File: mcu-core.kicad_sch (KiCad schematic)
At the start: 17 parts, among them SW1 B3U-1000P, U1 STM32F103C8T6, Y1 12MHz

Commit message: Modified gitignore
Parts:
- C2: value 4u7 -> 0u1
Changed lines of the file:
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@@
       (effects (font (size 1.27 1.27)) (justify left))
     )
-    (property "Value" "4u7" (id 1) (at 35.56 181.6162 0)
+    (property "Value" "0u1" (id 1) (at 35.56 181.6162 0)
       (effects (font (size 1.27 1.27)) (justify left))
     )

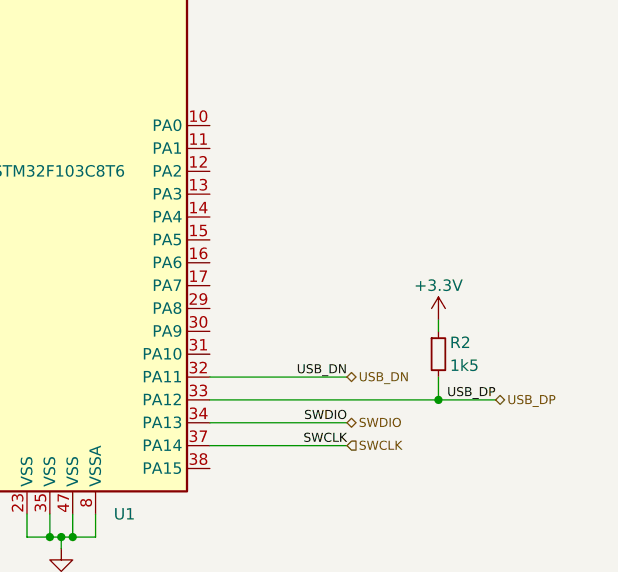
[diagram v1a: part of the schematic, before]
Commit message: Added connections for motor 2
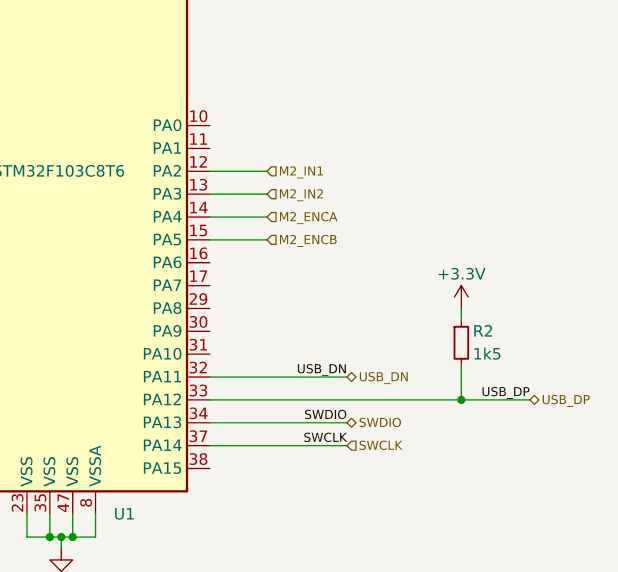
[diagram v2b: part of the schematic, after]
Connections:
- net M2_IN1: now reaches U1.12 (PA2)
- net M2_IN2: now reaches U1.13 (PA3)
- net M2_ENCA: now reaches U1.14 (PA4)
- net M2_ENCB: now reaches U1.15 (PA5)
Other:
- moved on the sheet: R2
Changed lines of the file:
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@@
   (junction (at 147.32 151.13) (diameter 0) (color 0 0 0 0)
   )
-  (junction (at 187.96 135.89) (diameter 0) (color 0 0 0 0)
+  (junction (at 190.5 135.89) (diameter 0) (color 0 0 0 0)
   )
   (junction (at 146.05 151.13) (diameter 0) (color 0 0 0 0)
@@
     (stroke (width 0) (type default) (color 0 0 0 0))
   )
-  (wire (pts (xy 162.56 135.89) (xy 187.96 135.89))
+  (wire (pts (xy 162.56 110.49) (xy 168.91 110.49))
+    (stroke (width 0) (type default) (color 0 0 0 0))
+  )
+  (wire (pts (xy 162.56 135.89) (xy 190.5 135.89))
     (stroke (width 0) (type default) (color 0 0 0 0))
   )
@@
     (stroke (width 0) (type default) (color 0 0 0 0))
   )
+  (wire (pts (xy 162.56 113.03) (xy 168.91 113.03))
+    (stroke (width 0) (type default) (color 0 0 0 0))
+  )
   (wire (pts (xy 133.35 59.69) (xy 133.35 58.42))
     (stroke (width 0) (type default) (color 0 0 0 0))
@@
     (stroke (width 0) (type default) (color 0 0 0 0))
   )
-  (wire (pts (xy 187.96 135.89) (xy 194.31 135.89))
+  (wire (pts (xy 190.5 135.89) (xy 198.12 135.89))
     (stroke (width 0) (type default) (color 0 0 0 0))
   )
@@
     (stroke (width 0) (type default) (color 0 0 0 0))
   )
-  (wire (pts (xy 187.96 127) (xy 187.96 128.27))
+  (wire (pts (xy 190.5 125.73) (xy 190.5 127))
     (stroke (width 0) (type default) (color 0 0 0 0))
   )
@@
     (stroke (width 0) (type default) (color 0 0 0 0))
   )
-  (wire (pts (xy 187.96 133.35) (xy 187.96 135.89))
+  (wire (pts (xy 162.56 115.57) (xy 168.91 115.57))
+    (stroke (width 0) (type default) (color 0 0 0 0))
+  )
+  (wire (pts (xy 190.5 132.08) (xy 190.5 135.89))
     (stroke (width 0) (type default) (color 0 0 0 0))
   )
@@
   )
   (wire (pts (xy 25.4 130.81) (xy 17.78 130.81))
+    (stroke (width 0) (type default) (color 0 0 0 0))
+  )
+  (wire (pts (xy 162.56 118.11) (xy 168.91 118.11))
     (stroke (width 0) (type default) (color 0 0 0 0))
   )
@@
     (effects (font (size 1 1)) (justify left bottom))
   )
-  (label "USB_DP" (at 194.31 135.89 180)
+  (label "USB_DP" (at 198.12 135.89 180)
     (effects (font (size 1 1)) (justify right bottom))
   )
@@
   (label "M1_IN2" (at 121.92 123.19 0)
     (effects (font (size 1 1)) (justify left bottom))
+  )
+  (hierarchical_label "M2_ENCB" (shape input) (at 168.91 118.11 0)
+    (effects (font (size 1 1)) (justify left))
   )
   (hierarchical_label "SWCLK" (shape input) (at 177.8 140.97 0)
@@
     (effects (font (size 1 1)) (justify left))
   )
-  (hierarchical_label "USB_DP" (shape bidirectional) (at 194.31 135.89 0)
+  (hierarchical_label "M2_IN2" (shape input) (at 168.91 113.03 0)
+    (effects (font (size 1 1)) (justify left))
+  )
+  (hierarchical_label "USB_DP" (shape bidirectional) (at 198.12 135.89 0)
     (effects (font (size 1 1)) (justify left))
   )
@@
   (hierarchical_label "M1_ENCA" (shape input) (at 121.92 118.11 180)
     (effects (font (size 1 1)) (justify right))
+  )
+  (hierarchical_label "M2_ENCA" (shape input) (at 168.91 115.57 0)
+    (effects (font (size 1 1)) (justify left))
+  )
+  (hierarchical_label "M2_IN1" (shape input) (at 168.91 110.49 0)
+    (effects (font (size 1 1)) (justify left))
   )
   (symbol (lib_id "Device:C_Small") (at 36.83 139.7 0) (unit 1)
@@
     (pin "2")
   )
-  (symbol (lib_id "Device:R_Small") (at 187.96 130.81 0) (unit 1)
+  (symbol (lib_id "Device:R_Small") (at 190.5 129.54 0) (unit 1)
     (in_bom yes) (on_board yes)
-    (property "Reference" "R2" (id 0) (at 189.23 129.54 0)
+    (property "Reference" "R2" (id 0) (at 191.77 128.27 0)
       (effects (font (size 1.27 1.27)) (justify left))
     )
-    (property "Value" "1k5" (id 1) (at 189.23 132.08 0)
+    (property "Value" "1k5" (id 1) (at 191.77 130.81 0)
       (effects (font (size 1.27 1.27)) (justify left))
     )
-    (property "Footprint" "Resistor_SMD:R_0402_1005Metric" (id 2) (at 187.96 130.81 0)
-      (effects (font (size 1.27 1.27)) hide)
-    )
-    (property "Datasheet" "~" (id 3) (at 187.96 130.81 0)
+    (property "Footprint" "Resistor_SMD:R_0402_1005Metric" (id 2) (at 190.5 129.54 0)
+      (effects (font (size 1.27 1.27)) hide)
+    )
+    (property "Datasheet" "~" (id 3) (at 190.5 129.54 0)
       (effects (font (size 1.27 1.27)) hide)
     )
@@
     (pin "4")
   )
-  (symbol (lib_id "power:+3.3V") (at 187.96 127 0) (unit 1)
+  (symbol (lib_id "power:+3.3V") (at 190.5 125.73 0) (unit 1)
     (in_bom yes) (on_board yes)
-    (property "Reference" "#PWR013" (id 0) (at 187.96 130.81 0)
-      (effects (font (size 1.27 1.27)) hide)
-    )
-    (property "Value" "+3.3V" (id 1) (at 187.96 123.19 0))
-    (property "Footprint" "" (id 2) (at 187.96 127 0)
-      (effects (font (size 1.27 1.27)) hide)
-    )
-    (property "Datasheet" "" (id 3) (at 187.96 127 0)
-      (effects (font (size 1.27 1.27)) hide)
-    )
+    (property "Reference" "#PWR013" (id 0) (at 190.5 129.54 0)
+      (effects (font (size 1.27 1.27)) hide)
+    )
+    (property "Value" "+3.3V" (id 1) (at 190.5 121.92 0))
+    (property "Footprint" "" (id 2) (at 190.5 125.73 0)
+      (effects (font (size 1.27 1.27)) hide)
+    )
+    (property "Datasheet" "" (id 3) (at 190.5 125.73 0)
+      (effects (font (size 1.27 1.27)) hide)
+    )
